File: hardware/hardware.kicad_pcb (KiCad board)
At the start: 2 copper layers, 33 parts, among them J1 USB_A, J3 SWD, J6 Conn_01x04, SW1 SW_Push, U1 MCP2551-I_SN, U2 LM317_SOT-223-3.3V, U3 STM32F107RBTx, U4 TJA1020, Y1 Crystal

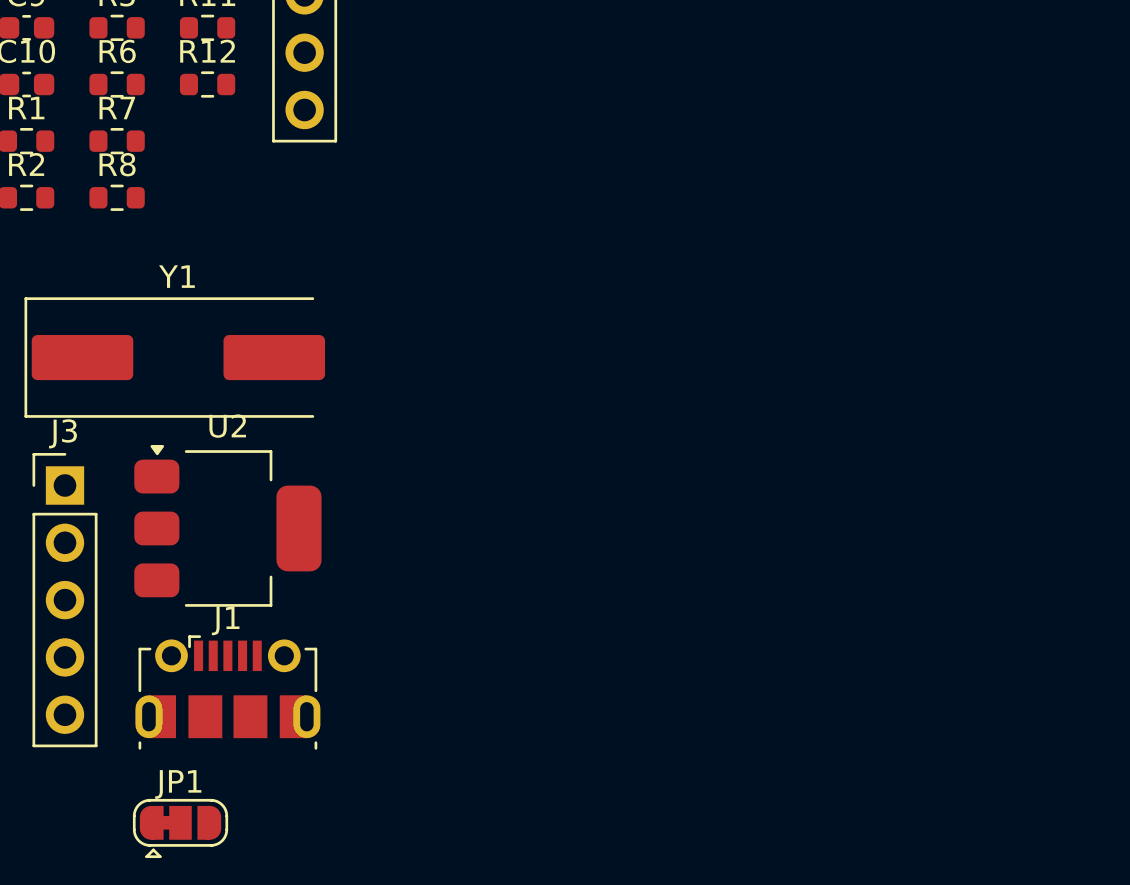
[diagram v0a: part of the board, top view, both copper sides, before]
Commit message: add lin + can connectors
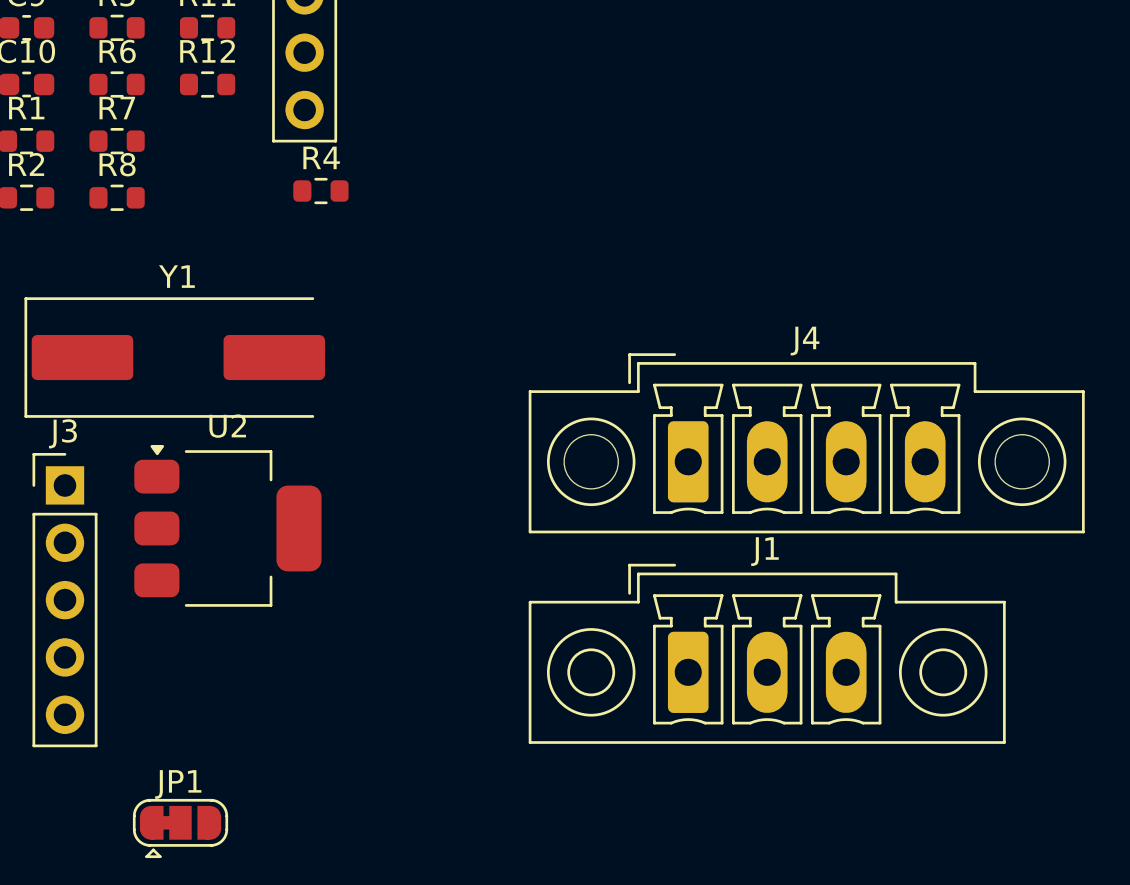
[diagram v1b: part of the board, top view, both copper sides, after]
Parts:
- added J4: Conn_01x04, Connector_Phoenix_MC:PhoenixContact_MCV_1,5_4-GF-3.5_1x04_P3.50mm_Vertical_ThreadedFlange_MountHole, F.Cu at (138.7, 87.8)
- added R4: 10k, Resistor_SMD:R_0603_1608Metric, F.Cu at (122.4, 75.8)
- J1: value USB_A -> Conn_01x03; footprint Connector_USB:USB_Micro-B_Molex-105017-0001 -> Connector_Phoenix_MC:PhoenixContact_MCV_1,5_3-GF-3.5_1x03_P3.50mm_Vertical_ThreadedFlange
- moved J1 20.4 mm to (138.7, 97.1)
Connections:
- C1 pad 1: +5V -> +VDC
- J1 pad 1: +5V -> Net-(J1-Pin_1)
- J1 pad 2: unconnected-(J1-D--Pad2) -> +VDC
- J1 pad 3: unconnected-(J1-D+-Pad3) -> GND
- U2 pad 3: +5V -> +VDC
- U3 pad 16: LED2 -> LIN_TX
- U3 pad 17: unconnected-(U3-PA3-Pad17) -> LIN_RX
- U3 pad 42: unconnected-(U3-PA9-Pad42) -> LED2
- U3 pad 55: unconnected-(U3-PB3-Pad55) -> LIN_INH
- U3 pad 56: unconnected-(U3-PB4-Pad56) -> LIN_WAKE
- U3 pad 57: unconnected-(U3-PB5-Pad57) -> LIN_EN
- U4 pad 1: unconnected-(U4-RXD-Pad1) -> LIN_RX
- U4 pad 2: unconnected-(U4-NSLP-Pad2) -> LIN_EN
- U4 pad 3: unconnected-(U4-NWAKE-Pad3) -> LIN_WAKE
- U4 pad 4: unconnected-(U4-TXD-Pad4) -> LIN_TX
- U4 pad 5: unconnected-(U4-GND-Pad5) -> GND
- U4 pad 6: unconnected-(U4-LIN-Pad6) -> Net-(J1-Pin_1)
- U4 pad 8: unconnected-(U4-INH-Pad8) -> LIN_INH

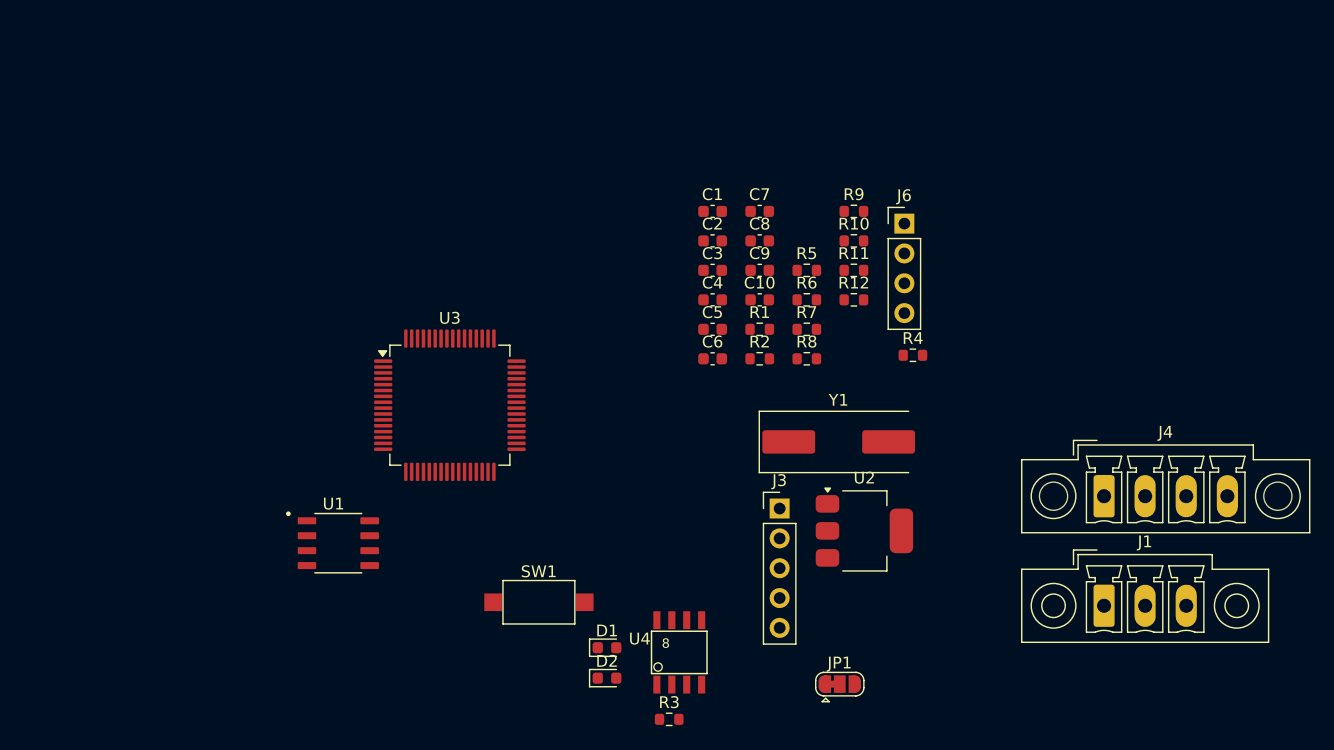
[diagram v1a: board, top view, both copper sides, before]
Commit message: fix boot 0 & boot 1 pin
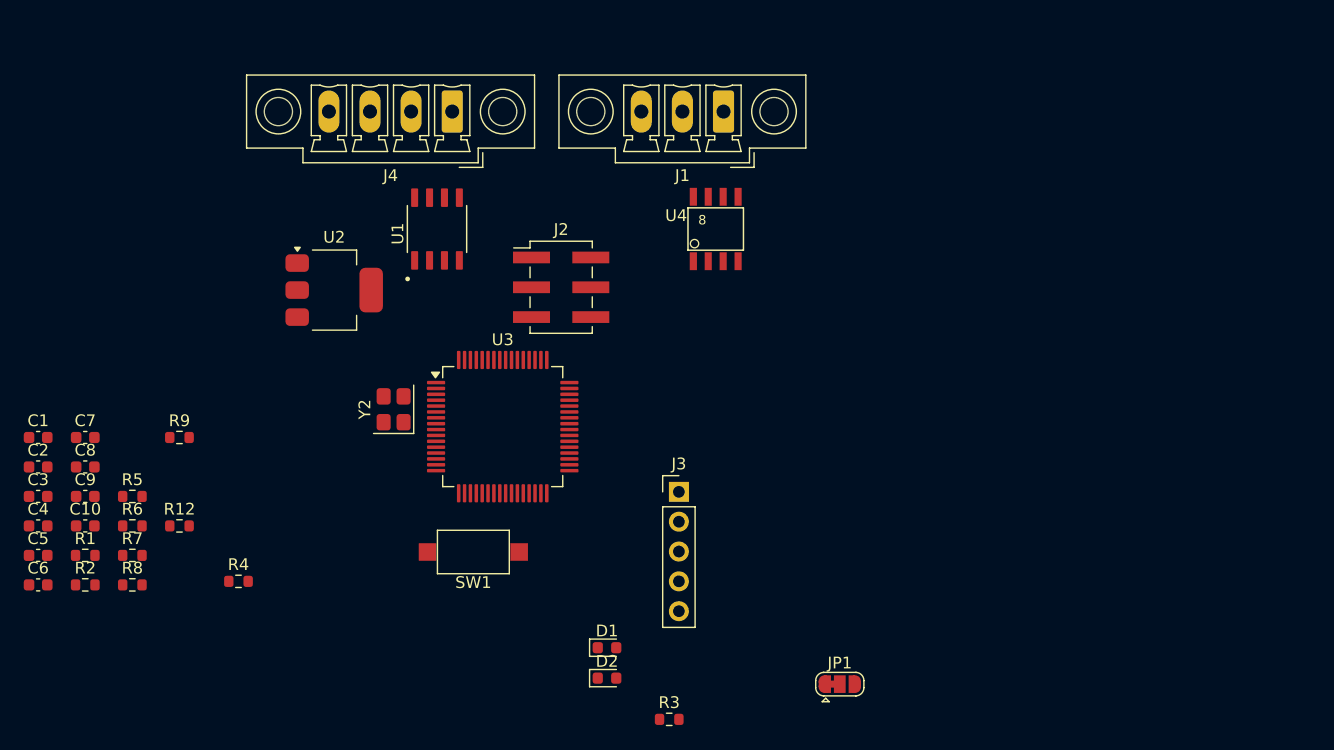
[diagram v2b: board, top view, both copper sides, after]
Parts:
- removed J6: Conn_01x04, Connector_PinHeader_2.54mm:PinHeader_1x04_P2.54mm_Vertical
- removed R10, R11: 10k, Resistor_SMD:R_0603_1608Metric
- removed Y1: Crystal, Crystal:Crystal_SMD_HC49-SD
- added J2: BOOT, Connector_PinHeader_2.54mm:PinHeader_2x03_P2.54mm_Vertical_SMD, F.Cu at (92.5, 70.0)
- added Y2: Crystal_GND24, Crystal:Crystal_SMD_3225-4Pin_3.2x2.5mm, F.Cu at (78.2, 80.3)
- J1: footprint Connector_Phoenix_MC:PhoenixContact_MCV_1,5_3-GF-3.5_1x03_P3.50mm_Vertical_ThreadedFlange -> Connector_Phoenix_MC:PhoenixContact_MCV_1,5_3-GF-3.5_1x03_P3.50mm_Vertical_ThreadedFlange_MountHole
- moved J4 64.4 mm to (83.2, 55.0), turned to 180 degrees
- moved C1 60.6 mm to (47.9, 82.8)
- moved C2 60.6 mm to (47.9, 85.3)
- moved C3 60.6 mm to (47.9, 87.8)
- moved C4 60.6 mm to (47.9, 90.3)
- moved C5 60.6 mm to (47.9, 92.8)
- moved C6 60.6 mm to (47.9, 95.3)
- moved R12 60.6 mm to (60.0, 90.3)
- moved R9 60.6 mm to (60.0, 82.8)
- moved C10 60.6 mm to (52.0, 90.3)
- moved C7 60.6 mm to (52.0, 82.8)
- moved C8 60.6 mm to (52.0, 85.3)
- moved C9 60.6 mm to (52.0, 87.8)
- moved R1 60.6 mm to (52.0, 92.8)
- moved R2 60.6 mm to (52.0, 95.3)
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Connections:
- U1 pad 6: Net-(J4-Pin_2) -> Net-(J4-Pin_1)
- U1 pad 7: Net-(J4-Pin_1) -> Net-(J4-Pin_2)

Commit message: finish pcb wiring
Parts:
- added ?: , , F.Cu at (68.0, 89.5)
- added ?: , , F.Cu at (112.0, 89.5)
- added REF**: MountingHole_3.2mm_M3_Pad, MountingHole:MountingHole_3.2mm_M3_Pad, F.Cu at (88.4, 63.3)
- J2: footprint Connector_PinHeader_2.54mm:PinHeader_2x03_P2.54mm_Vertical_SMD -> Connector_PinHeader_2.54mm:PinHeader_2x03_P2.54mm_Vertical
- moved R2 62.3 mm to (108.5, 69.1), turned to 180 degrees
- moved R1 60.7 mm to (108.5, 70.7)
- moved C6 59.4 mm to (102.3, 71.3), turned to 45 degrees
- moved R4 55.7 mm to (109.5, 61.5), turned to -90 degrees
- moved C5 55.2 mm to (95.0, 64.0), turned to 45 degrees
- moved R7 52.3 mm to (107.0, 81.5)
- moved R6 51.5 mm to (107.0, 83.2)
- moved C10 51.2 mm to (101.5, 77.5), turned to 135 degrees
- moved R3 49.7 mm to (78.0, 63.0), turned to -90 degrees
- moved C9 44.9 mm to (96.5, 82.5), turned to -45 degrees
- moved C7 41.1 mm to (93.0, 82.0), turned to -135 degrees
- moved R12 40.7 mm to (100.0, 83.0), turned to 45 degrees
- moved C4 40.0 mm to (84.0, 73.0), turned to -135 degrees
- moved D2 37.2 mm to (69.0, 78.0), turned to 180 degrees
- moved D1 33.1 mm to (69.0, 82.0), turned to 180 degrees
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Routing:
- net +3.3V: track 0.00 -> 130.1 mm, vias 0 -> 22
- net +VDC: track 0.00 -> 65.1 mm
- net RESET: track 0.00 -> 46.6 mm, vias 0 -> 3
- net SWCLK: track 0.00 -> 36.4 mm, vias 0 -> 2
- net SWDIO: track 0.00 -> 34.2 mm, vias 0 -> 2
- net LED1: track 0.00 -> 31.9 mm, vias 0 -> 2
- net LED2: track 0.00 -> 25.3 mm, vias 0 -> 2
- net BOOT0: track 0.00 -> 22.2 mm, vias 0 -> 2
- net GND: track 0.00 -> 22.0 mm, vias 0 -> 16
- net LIN_WAKE: track 0.00 -> 21.9 mm, vias 0 -> 2
- net LIN_INH: track 0.00 -> 21.8 mm, vias 0 -> 2
- net LIN_EN: track 0.00 -> 19.8 mm, vias 0 -> 2
- net BOOT1: track 0.00 -> 18.8 mm, vias 0 -> 2
- net CAN_TX: track 0.00 -> 11.6 mm
- net Net-(J1-Pin_1): track 0.00 -> 11.0 mm
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- added copper zone on B.Cu, net +3.3V
- added copper zone on F.Cu, net +3.3V
- added copper zone on B.Cu, net GND
- added copper zone on F.Cu, net GND
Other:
- board outline added: 50 x 42.5 mm
